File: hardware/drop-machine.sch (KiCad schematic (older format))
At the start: 22 parts

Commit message: Update schematics to match actual construction
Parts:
- removed J?: CONN_02X10, symbol CONN_02X10
- added J?: CONN_01X06, symbol CONN_01X06
- added J?: Indicator, symbol CONN_01X02
- added R?: 1k, symbol R
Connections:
- wire segments 46 -> 47
- no-connect marks 8 -> 7
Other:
- moved on the sheet: D?, J?, R?
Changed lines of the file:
@@
 L LED D?
 U 1 1 5A7A559B
-P 6100 3050
-F 0 "D?" H 6100 3150 50  0000 C CNN
-F 1 "LED" H 6100 2950 50  0000 C CNN
-F 2 "" H 6100 3050 50  0001 C CNN
-F 3 "" H 6100 3050 50  0001 C CNN
-	1    6100 3050
+P 6450 4900
+F 0 "D?" H 6450 5000 50  0000 C CNN
+F 1 "LED" H 6450 4800 50  0000 C CNN
+F 2 "" H 6450 4900 50  0001 C CNN
+F 3 "" H 6450 4900 50  0001 C CNN
+	1    6450 4900
 	-1   0    0    1
 $EndComp
@@
 L R R?
 U 1 1 5A7A55D0
-P 5800 3050
-F 0 "R?" V 5880 3050 50  0000 C CNN
-F 1 "1k" V 5800 3050 50  0000 C CNN
-F 2 "" V 5730 3050 50  0001 C CNN
-F 3 "" H 5800 3050 50  0001 C CNN
-	1    5800 3050
+P 6150 4900
+F 0 "R?" V 6230 4900 50  0000 C CNN
+F 1 "1k" V 6150 4900 50  0000 C CNN
+F 2 "" V 6080 4900 50  0001 C CNN
+F 3 "" H 6150 4900 50  0001 C CNN
+	1    6150 4900
 	0    1    1    0
 $EndComp
@@
 L GND #PWR04
 U 1 1 5A7A55FF
-P 6250 3050
-F 0 "#PWR04" H 6250 2800 50  0001 C CNN
-F 1 "GND" H 6250 2900 50  0000 C CNN
-F 2 "" H 6250 3050 50  0001 C CNN
-F 3 "" H 6250 3050 50  0001 C CNN
-	1    6250 3050
+P 6600 4900
+F 0 "#PWR04" H 6600 4650 50  0001 C CNN
+F 1 "GND" H 6600 4750 50  0000 C CNN
+F 2 "" H 6600 4900 50  0001 C CNN
+F 3 "" H 6600 4900 50  0001 C CNN
+	1    6600 4900
 	1    0    0    -1
 $EndComp
@@
 L CONN_02X03 J?
 U 1 1 5A7D942B
-P 6600 4100
-F 0 "J?" H 6600 4300 50  0000 C CNN
-F 1 "Isp_conn" H 6600 3900 50  0000 C CNN
-F 2 "" H 6600 2900 50  0001 C CNN
-F 3 "" H 6600 2900 50  0001 C CNN
-	1    6600 4100
+P 7000 4100
+F 0 "J?" H 7000 4300 50  0000 C CNN
+F 1 "Isp_conn" H 7000 3900 50  0000 C CNN
+F 2 "" H 7000 2900 50  0001 C CNN
+F 3 "" H 7000 2900 50  0001 C CNN
+	1    7000 4100
 	1    0    0    -1
 $EndComp
@@
 L +5V #PWR010
 U 1 1 5A7DA995
-P 6850 4000
-F 0 "#PWR010" H 6850 3850 50  0001 C CNN
-F 1 "+5V" H 6850 4140 50  0000 C CNN
-F 2 "" H 6850 4000 50  0001 C CNN
-F 3 "" H 6850 4000 50  0001 C CNN
-	1    6850 4000
+P 7250 4000
+F 0 "#PWR010" H 7250 3850 50  0001 C CNN
+F 1 "+5V" H 7250 4140 50  0000 C CNN
+F 2 "" H 7250 4000 50  0001 C CNN
+F 3 "" H 7250 4000 50  0001 C CNN
+	1    7250 4000
 	1    0    0    -1
 $EndComp
@@
 L GND #PWR011
 U 1 1 5A7DA9BF
-P 7000 4200
-F 0 "#PWR011" H 7000 3950 50  0001 C CNN
-F 1 "GND" H 7000 4050 50  0000 C CNN
-F 2 "" H 7000 4200 50  0001 C CNN
-F 3 "" H 7000 4200 50  0001 C CNN
-	1    7000 4200
+P 7400 4200
+F 0 "#PWR011" H 7400 3950 50  0001 C CNN
+F 1 "GND" H 7400 4050 50  0000 C CNN
+F 2 "" H 7400 4200 50  0001 C CNN
+F 3 "" H 7400 4200 50  0001 C CNN
+	1    7400 4200
 	1    0    0    -1
 $EndComp
@@
 L +12V #PWR017
 U 1 1 5A818868
-P 9500 4000
-F 0 "#PWR017" H 9500 3850 50  0001 C CNN
-F 1 "+12V" H 9500 4140 50  0000 C CNN
-F 2 "" H 9500 4000 50  0001 C CNN
-F 3 "" H 9500 4000 50  0001 C CNN
-	1    9500 4000
+P 9000 4000
+F 0 "#PWR017" H 9000 3850 50  0001 C CNN
+F 1 "+12V" H 9000 4140 50  0000 C CNN
+F 2 "" H 9000 4000 50  0001 C CNN
+F 3 "" H 9000 4000 50  0001 C CNN
+	1    9000 4000
 	1    0    0    -1
 $EndComp
@@
 NoConn ~ 5650 3800
 NoConn ~ 5650 4800
-NoConn ~ 5650 4900
 $Comp
 L C C?
@@
 NoConn ~ 3350 3700
 NoConn ~ 3350 3900
-$Comp
-L CONN_02X10 J?
-U 1 1 5A81D8F6
-P 8750 3750
-F 0 "J?" H 8750 4300 50  0000 C CNN
-F 1 "CONN_02X10" V 8750 3750 50  0000 C CNN
-F 2 "" H 8750 2550 50  0001 C CNN
-F 3 "" H 8750 2550 50  0001 C CNN
-	1    8750 3750
-	0    -1   -1   0
-$EndComp
-Wire Wire Line
-	5650 3400 5650 3050
+Wire Wire Line
+	5650 2550 5650 3400
 Wire Wire Line
 	2100 1800 2900 1800
@@
 	2100 1500 1800 1500
 Wire Wire Line
-	5650 4000 6350 4000
-Wire Wire Line
-	5650 4100 6350 4100
-Wire Wire Line
-	6350 4200 6200 4200
-Wire Wire Line
-	6200 5600 3100 5600
+	5650 4000 6750 4000
+Wire Wire Line
+	5650 4100 6750 4100
+Wire Wire Line
+	6750 4200 6750 4200
+Wire Wire Line
+	6750 5600 3100 5600
 Wire Wire Line
 	3100 5600 3100 3400
@@
 	3100 3400 3350 3400
 Wire Wire Line
-	7000 4200 6850 4200
-Wire Wire Line
-	6200 4200 6200 5600
+	7400 4200 7250 4200
+Wire Wire Line
+	6750 4200 6750 5600
 Wire Wire Line
 	5650 3900 6200 3900
@@
 	6200 3900 6200 3700
 Wire Wire Line
-	6200 3700 7000 3700
-Wire Wire Line
-	7000 3700 7000 4100
-Wire Wire Line
-	7000 4100 6850 4100
+	6200 3700 7400 3700
+Wire Wire Line
+	7400 3700 7400 4100
+Wire Wire Line
+	7400 4100 7250 4100
 Wire Wire Line
 	7700 4500 7700 4000
@@
 Wire Wire Line
 	5800 4700 5650 4700
-Connection ~ 9200 4000
-Connection ~ 9100 4000
-Wire Wire Line
-	9000 4000 9500 4000
-Wire Wire Line
-	9300 3500 9300 4000
-Wire Wire Line
-	9000 3500 9300 3500
-Connection ~ 9300 4000
-Connection ~ 9200 3500
-Connection ~ 9100 3500
 Wire Wire Line
 	1300 1500 1400 1500
+$Comp
+L CONN_01X06 J?
+U 1 1 5A82BF27
+P 8550 3800
+F 0 "J?" H 8550 4150 50  0000 C CNN
+F 1 "CONN_01X06" V 8650 3800 50  0000 C CNN
+F 2 "" H 8550 3800 50  0001 C CNN
+F 3 "" H 8550 3800 50  0001 C CNN
+	1    8550 3800
+	0    -1   -1   0
+$EndComp
+Wire Wire Line
+	8800 4000 9000 4000
+$Comp
+L R R?
+U 1 1 5A82C207
+P 6150 4400
+F 0 "R?" V 6230 4400 50  0000 C CNN
+F 1 "1k" V 6150 4400 50  0000 C CNN
+F 2 "" V 6080 4400 50  0001 C CNN
+F 3 "" H 6150 4400 50  0001 C CNN
+	1    6150 4400
+	0    1    1    0
+$EndComp
+$Comp
+L CONN_01X02 J?
+U 1 1 5A82C278
+P 6550 4450
+F 0 "J?" H 6550 4600 50  0000 C CNN
+F 1 "Indicator" V 6650 4450 50  0000 C CNN
+F 2 "" H 6550 4450 50  0001 C CNN
+F 3 "" H 6550 4450 50  0001 C CNN
+	1    6550 4450
+	1    0    0    -1
+$EndComp
+$Comp
+L GND #PWR?
+U 1 1 5A82C365
+P 6350 4500
+F 0 "#PWR?" H 6350 4250 50  0001 C CNN
+F 1 "GND" H 6350 4350 50  0000 C CNN
+F 2 "" H 6350 4500 50  0001 C CNN
+F 3 "" H 6350 4500 50  0001 C CNN
+	1    6350 4500
+	1    0    0    -1
+$EndComp
+Connection ~ 5650 3050
+Wire Wire Line
+	6300 4400 6350 4400
+Wire Wire Line
+	6000 4400 6000 4900
+Wire Wire Line
+	6000 4900 5650 4900
 $EndSCHEMATC

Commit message: Some library change automatically done by KiCad
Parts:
- SW?: symbol SW_SPST -> SW_SPST-RESCUE-drop-machine
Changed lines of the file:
@@
 EESchema Schematic File Version 2
+LIBS:drop-machine-rescue
 LIBS:power
 LIBS:device
@@
 $EndComp
 $Comp
-L SW_SPST SW?
+L SW_SPST-RESCUE-drop-machine SW?
 U 1 1 5A7ACC71
 P 1600 1500

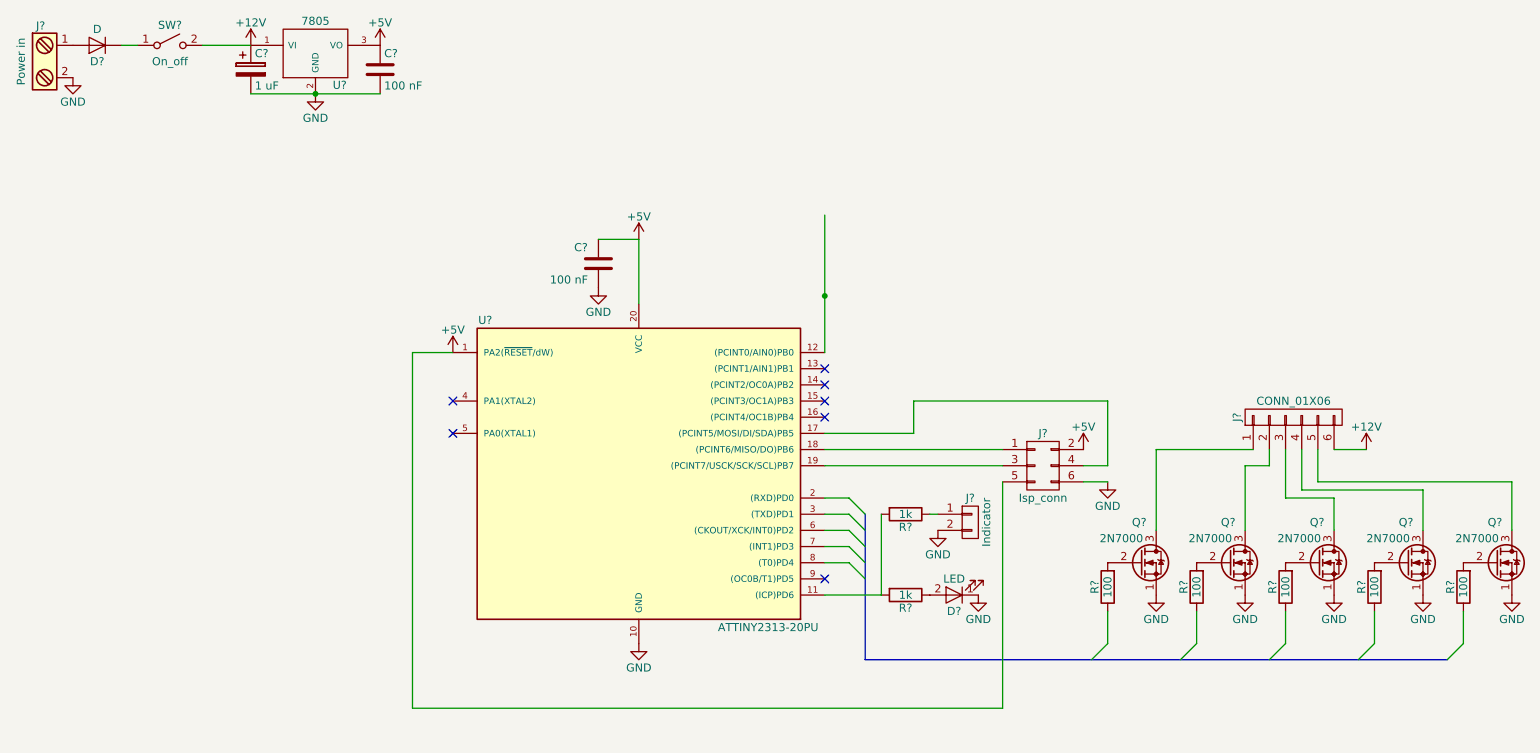
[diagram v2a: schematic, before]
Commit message: Add two more valves to create vertices of a hexagon and its middle
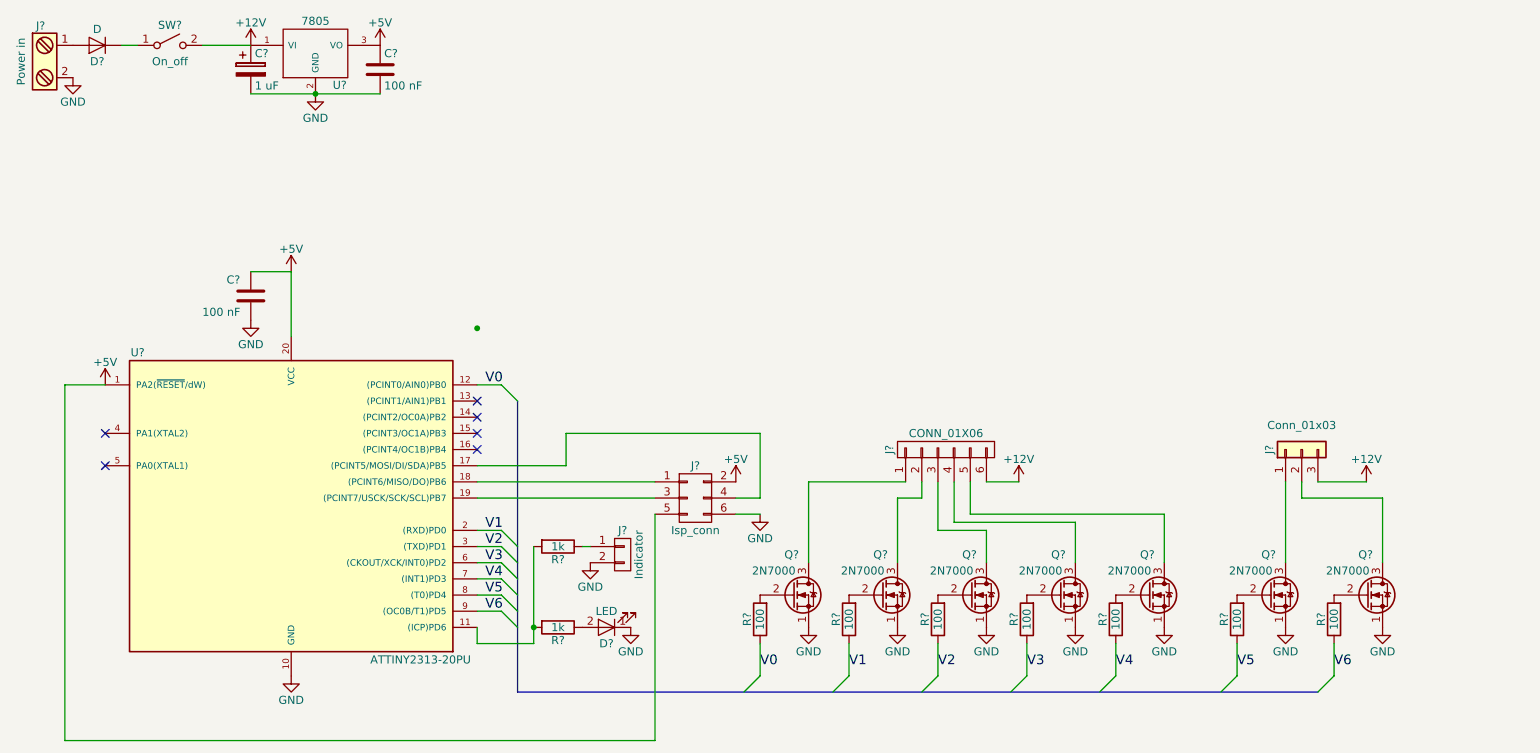
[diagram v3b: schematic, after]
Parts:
- added J?: Conn_01x03, symbol Conn_01x03
- added Q? (x2): 2N7000, symbol Q_NMOS_SGD
- added R? (x2): 100, symbol R
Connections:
- net +12V: now also J?.3 (Pin_3)
- net GND: now also Q?.1 (S), Q?.1 (S)
- net V0: now reaches U?.12 ((PCINT0/AIN0)PB0)
- net V0: now also R?.1
- net V1: now reaches U?.2 ((RXD)PD0)
- net V1: now also R?.1
- net V2: now reaches U?.3 ((TXD)PD1)
- net V2: now also R?.1
- net V3: now reaches U?.6 ((CKOUT/XCK/INT0)PD2)
- net V3: now also R?.1
- net V4: now reaches U?.7 ((INT1)PD3)
- net V4: now also R?.1
- net V5: now reaches U?.8 ((T0)PD4)
- net V5: now also R?.1
- net V6: now reaches U?.9 ((OC0B/T1)PD5)
- net V6: now also R?.1
- new net: Q?.2 (G), R?.2 (x2)
- new net: J?.1 (Pin_1), Q?.3 (D)
- new net: J?.2 (Pin_2), Q?.3 (D)
- no-connect marks 7 -> 6
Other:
- moved on the sheet: C?, D?, J?, Q?, R?, U?
